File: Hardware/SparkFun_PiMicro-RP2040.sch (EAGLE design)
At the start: 55 parts, among them J2 Qwiic, J5 USB Female Type C Connector, U1 3.3V, U2 RP2040, U3 WS2812-2020, U4 W25QXX128MBIT, Y1 12MHz

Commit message: Cleaning up schematic
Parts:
- removed FRAME1: FRAME-LETTER, SparkFun-Aesthetics:FRAME-LETTER
- added FRAME2: FRAME-LEDGER, SparkFun-Aesthetics:FRAME-LEDGER
- R14: value 200OHM-0402T-1/16W-1% -> 200
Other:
- note added: "Boot / Reset Buttons"
- note added: "Connections"
- note added: "Power Select and Regulation"
- note added: "USB"
- note added: "v11"
- note removed: "Arduino Pro Mini Design by Spark Fun Electronics"
- note removed: "Original Arduino Mini Design by Team Arduino"
- note removed: "Pro Micro Design by Spark Fun Electronics"
- note removed: "group pins silk together"
- note removed: "v20"
- moved on the sheet: C11, C12, C13, C14, C15, C16, C17, C18, C19, C20, C21, C22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

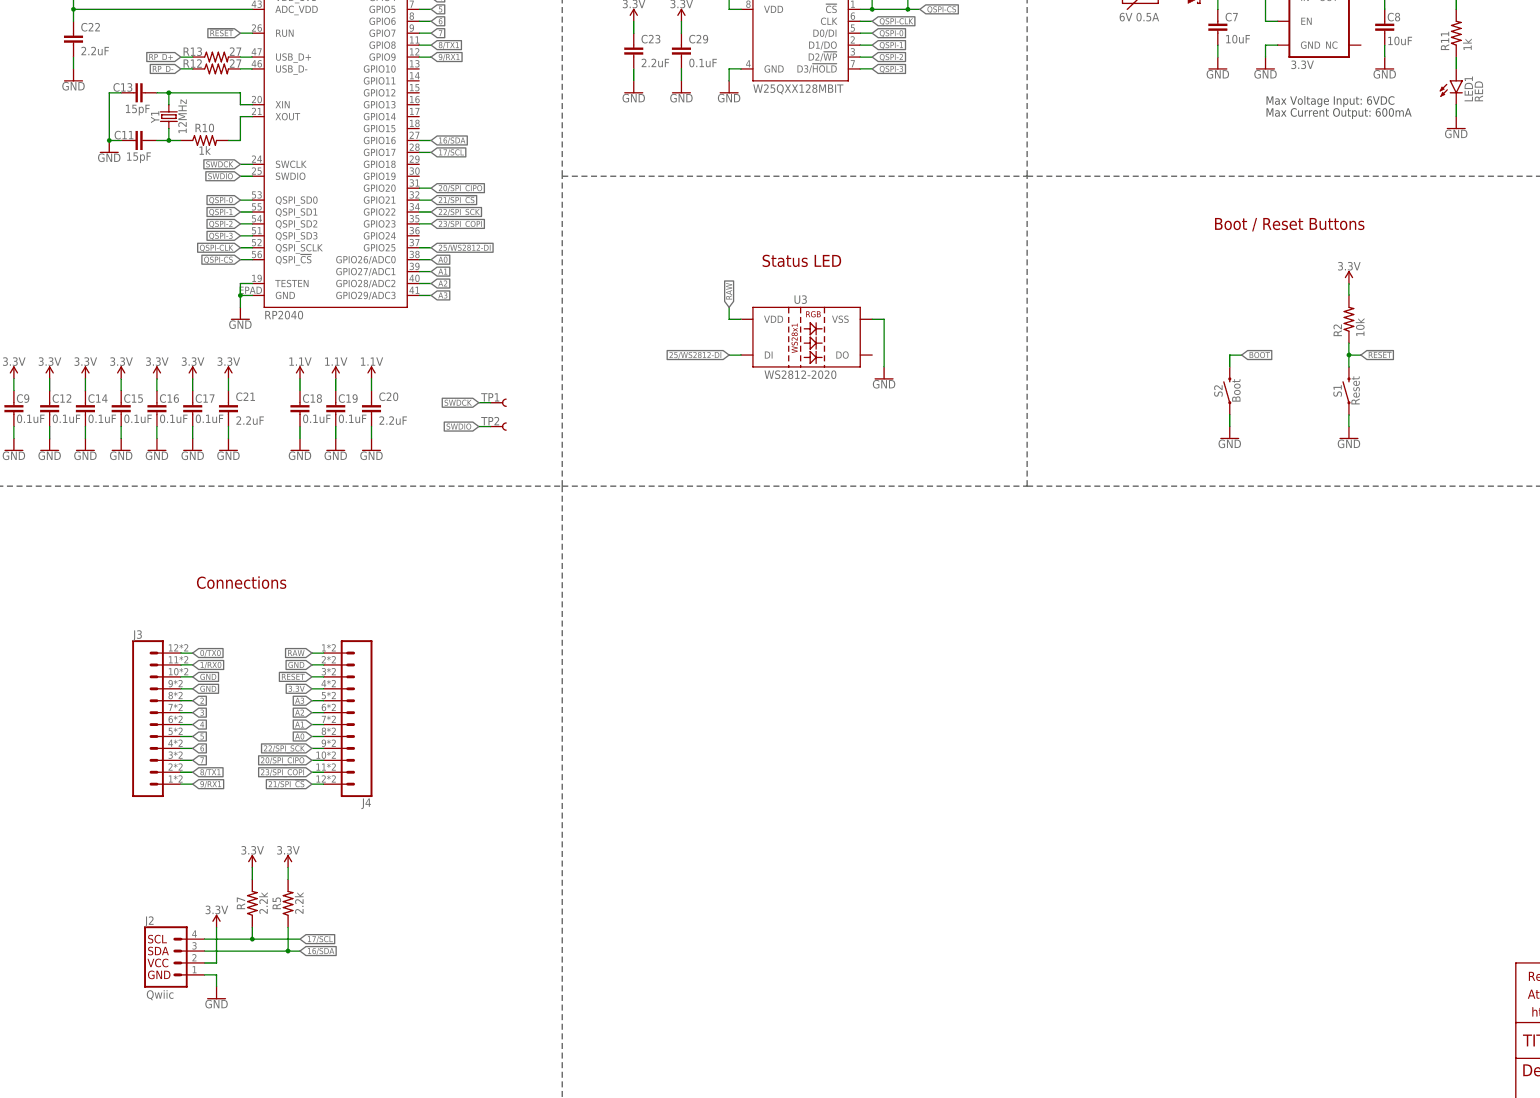
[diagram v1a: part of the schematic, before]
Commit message: Add RAW max voltage warning
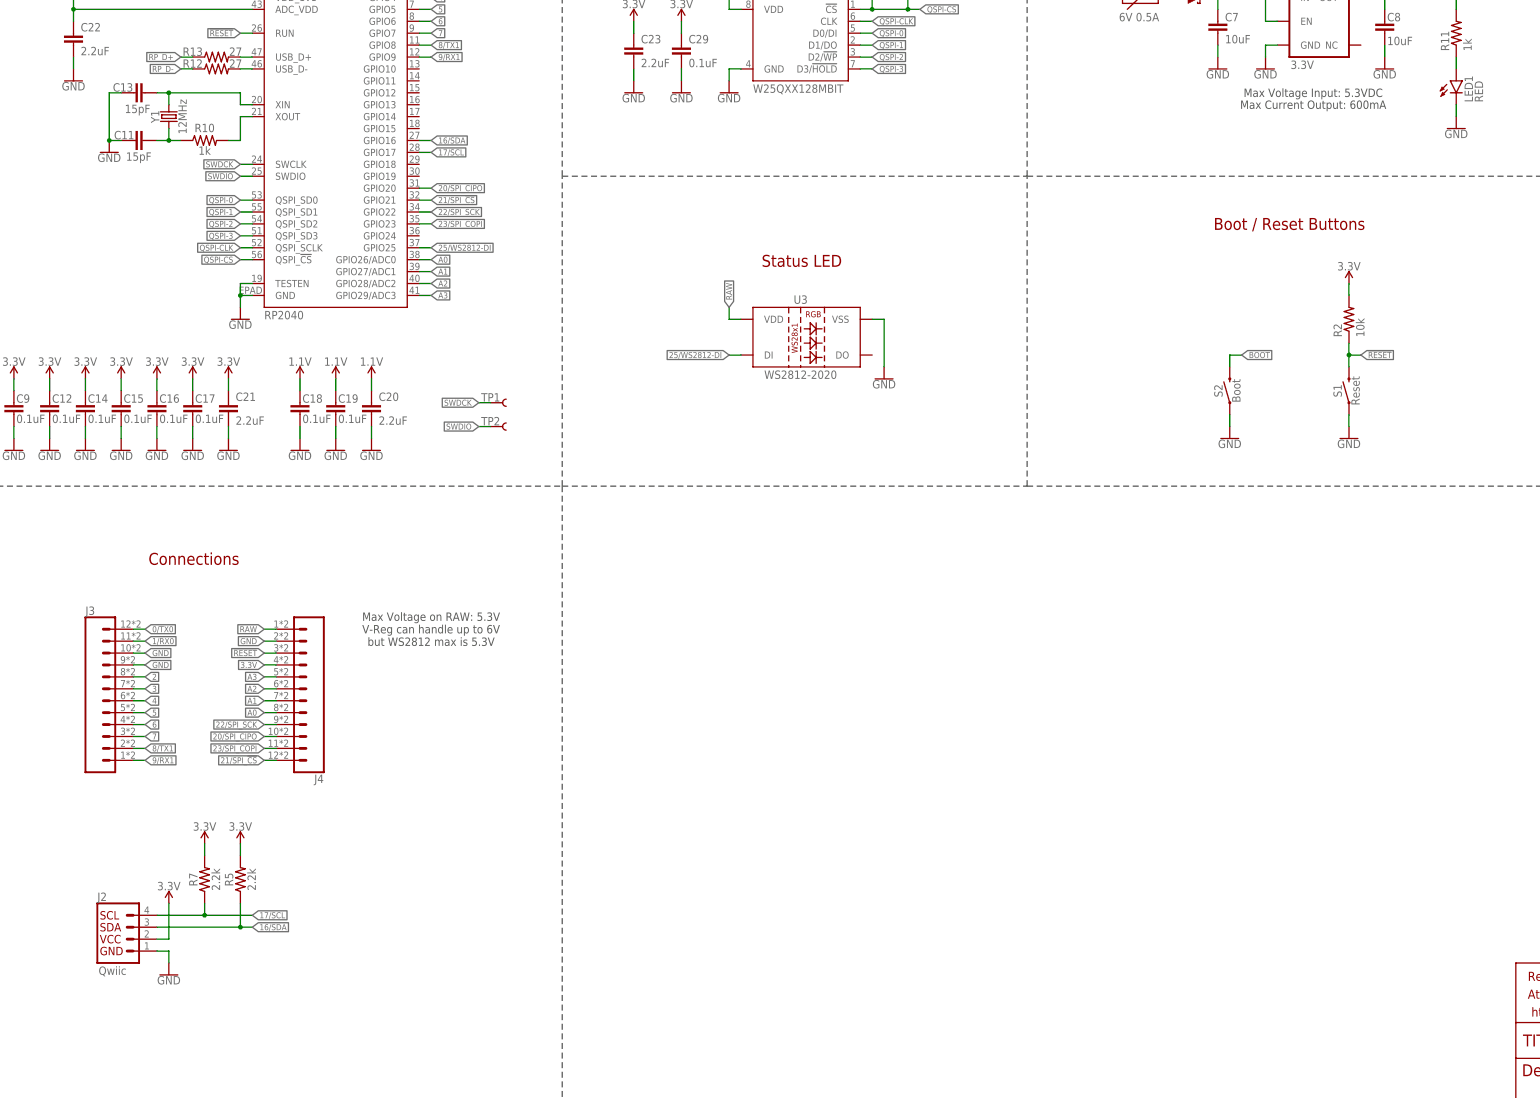
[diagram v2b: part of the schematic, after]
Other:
- note added: "Max Voltage Input: 5.3VDC"
- note added: "Max Voltage on RAW: 5.3V V-Reg can handle up to 6V but WS2812 max is 5.3V"
- note removed: "Max Voltage Input: 6VDC"
- moved on the sheet: J2, J3, J4, R5, R7

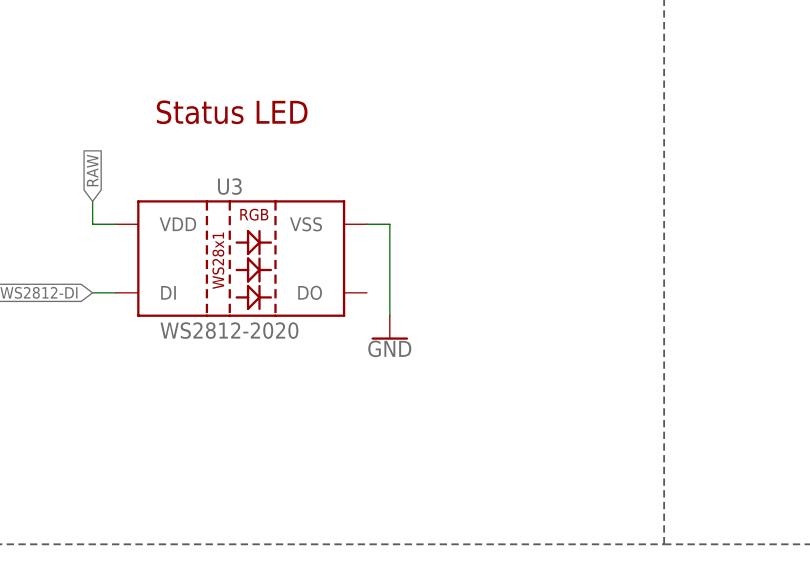
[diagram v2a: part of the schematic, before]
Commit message: Add DO TP for WS2812
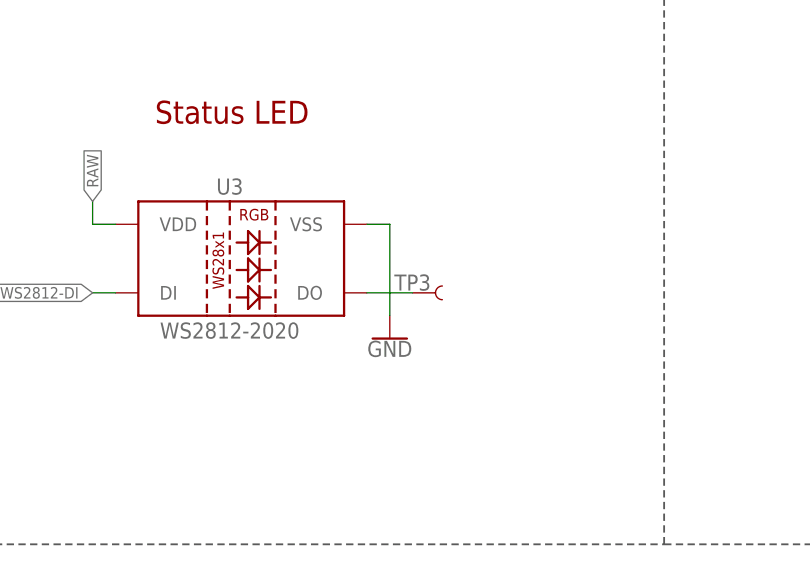
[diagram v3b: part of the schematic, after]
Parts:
- added TP3: TEST-POINT3X5, SparkFun-Connectors:TEST-POINT3X5
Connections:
- new net N$1: TP3.1, U3.DO
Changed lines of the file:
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@@
 <part name="GND4" library="SparkFun-PowerSymbols" deviceset="GND" device=""/>
 <part name="FRAME2" library="SparkFun-Aesthetics" deviceset="FRAME-LEDGER" device=""/>
+<part name="TP3" library="SparkFun-Connectors" deviceset="TEST-POINT" device="3X5" value=""/>
 </parts>
 <sheets>
@@
 <attribute name="REV" x="419.1" y="6.604" size="2.7432" layer="94" font="vector"/>
 </instance>
+<instance part="TP3" gate="G$1" x="198.12" y="165.1" smashed="yes">
+<attribute name="NAME" x="196.088" y="165.354" size="1.778" layer="95" font="vector"/>
+<attribute name="VALUE" x="195.58" y="162.56" size="1.778" layer="96" font="vector"/>
+</instance>
 </instances>
 <busses>
@@
 </segment>
 </net>
+<net name="N$1" class="0">
+<segment>
+<pinref part="U3" gate="G$1" pin="DO"/>
+<pinref part="TP3" gate="G$1" pin="1"/>
+<wire x1="193.04" y1="165.1" x2="198.12" y2="165.1" width="0.1524" layer="91"/>
+</segment>
+</net>
